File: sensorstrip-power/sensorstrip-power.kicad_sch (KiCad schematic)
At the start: 11 parts, among them J1 USB_C_Receptacle_PowerOnly, J2 Conn_01x02_MountingPin, SW1 SW_DPDT_x2

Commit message: fix humongous oversight
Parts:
- removed D1, D2, D3: LED, sensorstrip:LED_THT-1.27mm-OrthogonalSMDAndTHT, symbol Device:LED
- removed R1: 120R, Resistor_SMD:R_0805_2012Metric_Pad1.20x1.40mm_HandSolder, symbol Device:R
- added J3, J4, J5: Conn_01x02_MountingPin, Connector_Molex:Molex_PicoBlade_53261-0271_1x02-1MP_P1.25mm_Horizontal, symbol Connector_Generic_MountingPin:Conn_01x02_MountingPin
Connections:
- net GND: now also J3.2 (Pin_2), J3.MP (MountPin), J4.2 (Pin_2), J4.MP (MountPin), J5.2 (Pin_2), J5.MP (MountPin)
- net Power_postSwitch: now also J3.1 (Pin_1), J4.1 (Pin_1), J5.1 (Pin_1)

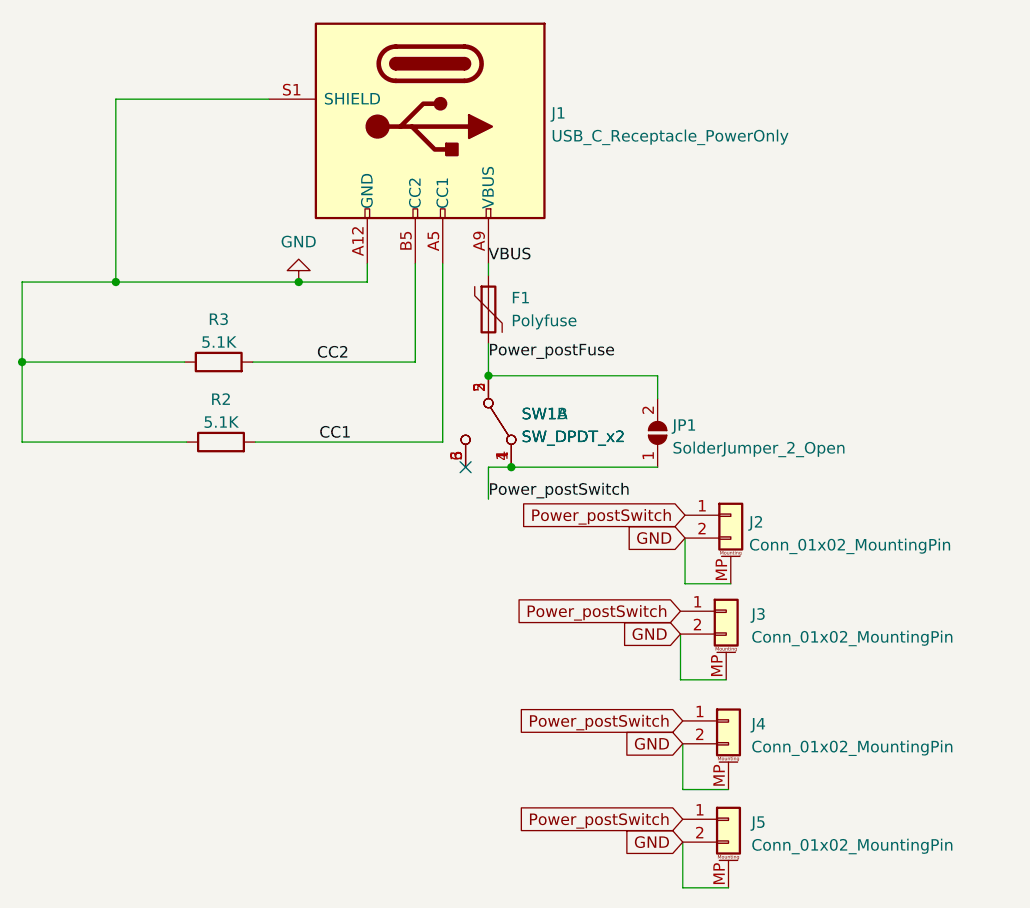
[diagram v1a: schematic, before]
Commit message: Cleanup in preparation for push
Update project files to KiCad 7 format
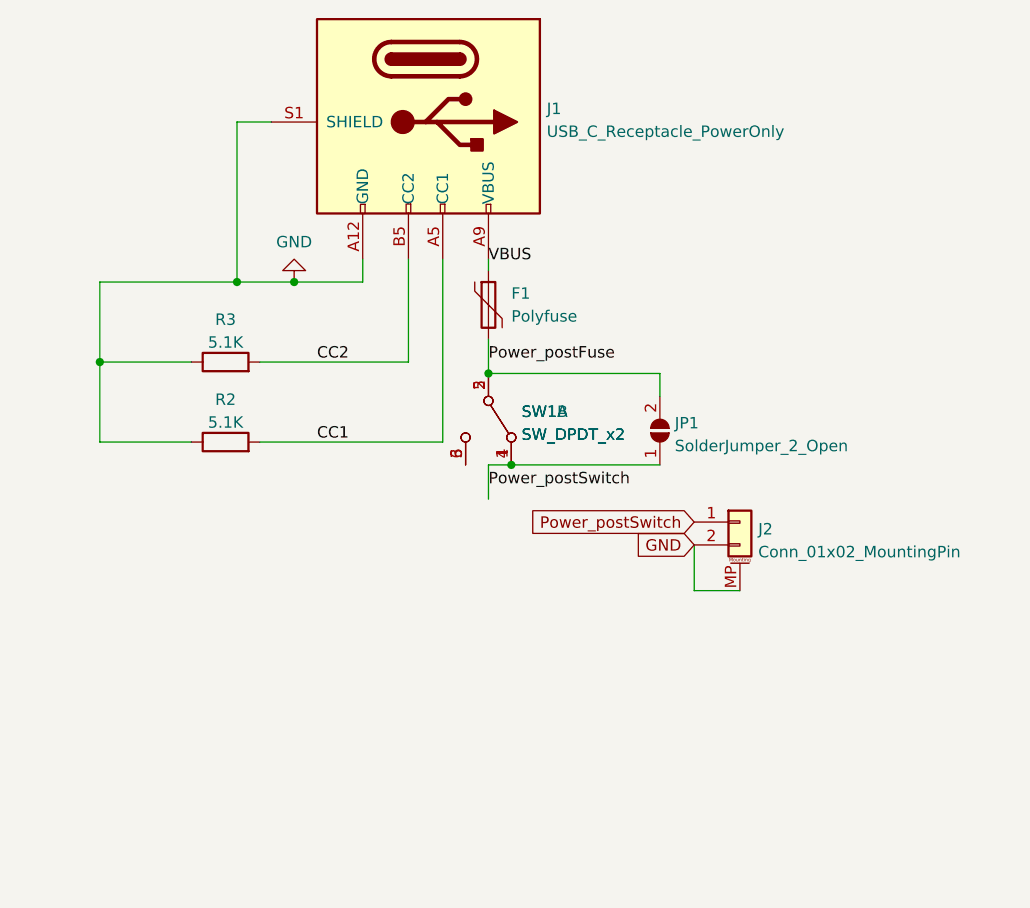
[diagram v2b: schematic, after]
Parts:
- removed J3, J4, J5: Conn_01x02_MountingPin, Connector_Molex:Molex_PicoBlade_53261-0271_1x02-1MP_P1.25mm_Horizontal, symbol Connector_Generic_MountingPin:Conn_01x02_MountingPin
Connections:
- no-connect marks 1 -> 0
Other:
- moved on the sheet: F1, J1, J2, R2, R3
